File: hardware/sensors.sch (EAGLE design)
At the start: 28 parts, among them J1 CDH, J2 OW, J3 DBG, J4 SUN-UART, J5 ADCS, J6 ENV, J7 SUN, U1 DS18B20, U2 DS18B20, U3 DS18B20

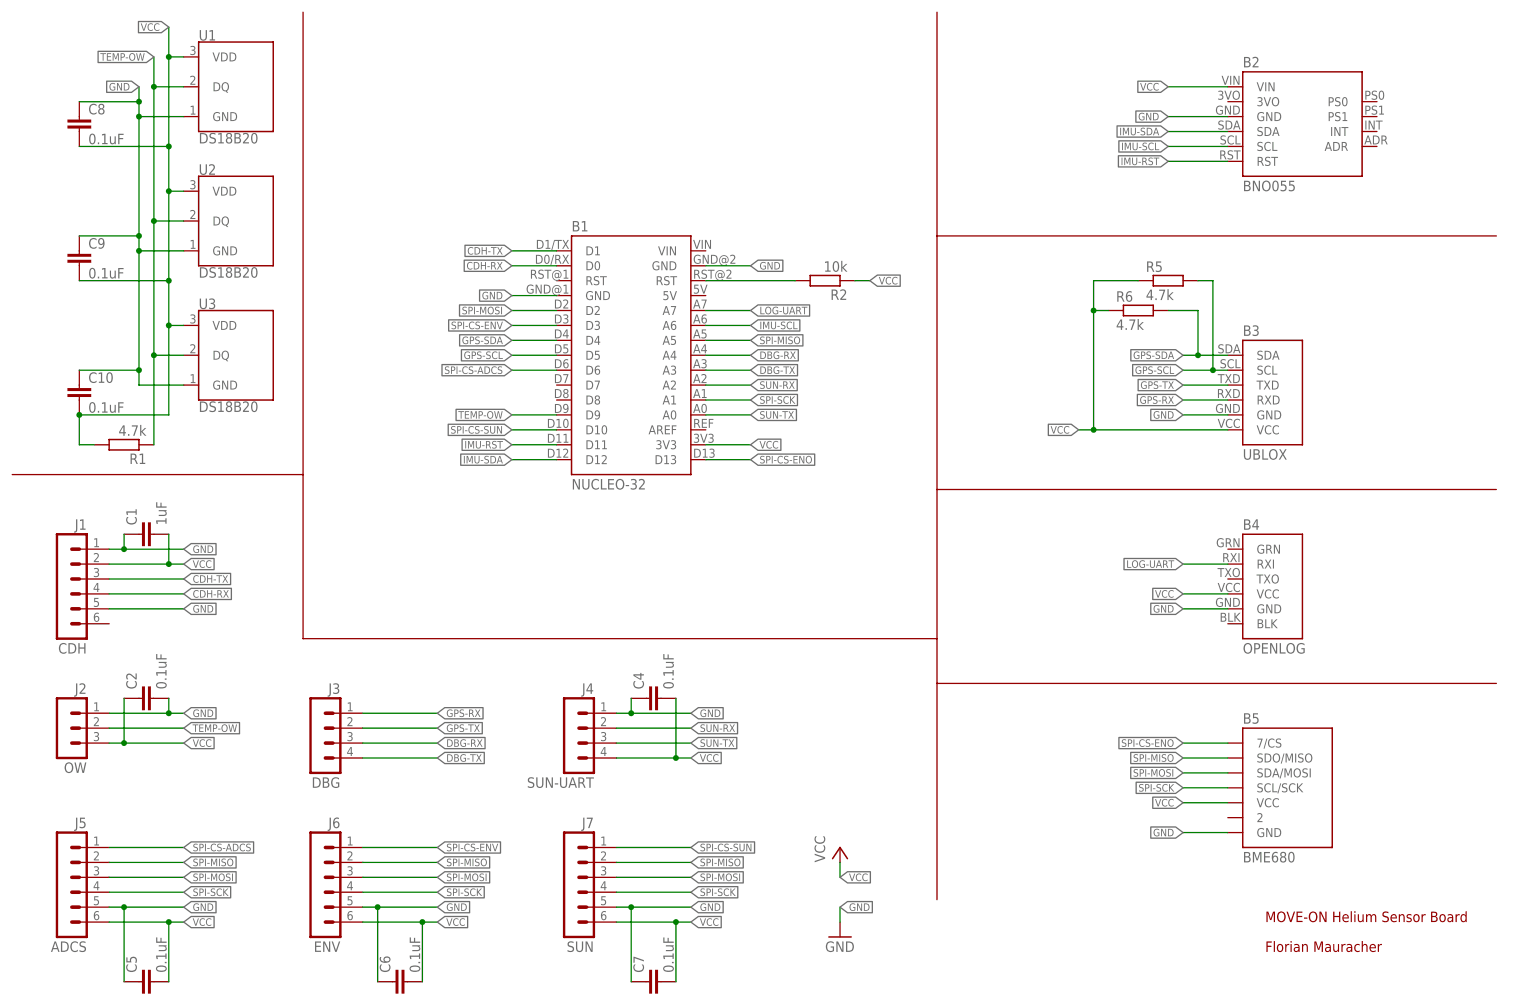
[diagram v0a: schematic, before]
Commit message: Update pin names to match sw
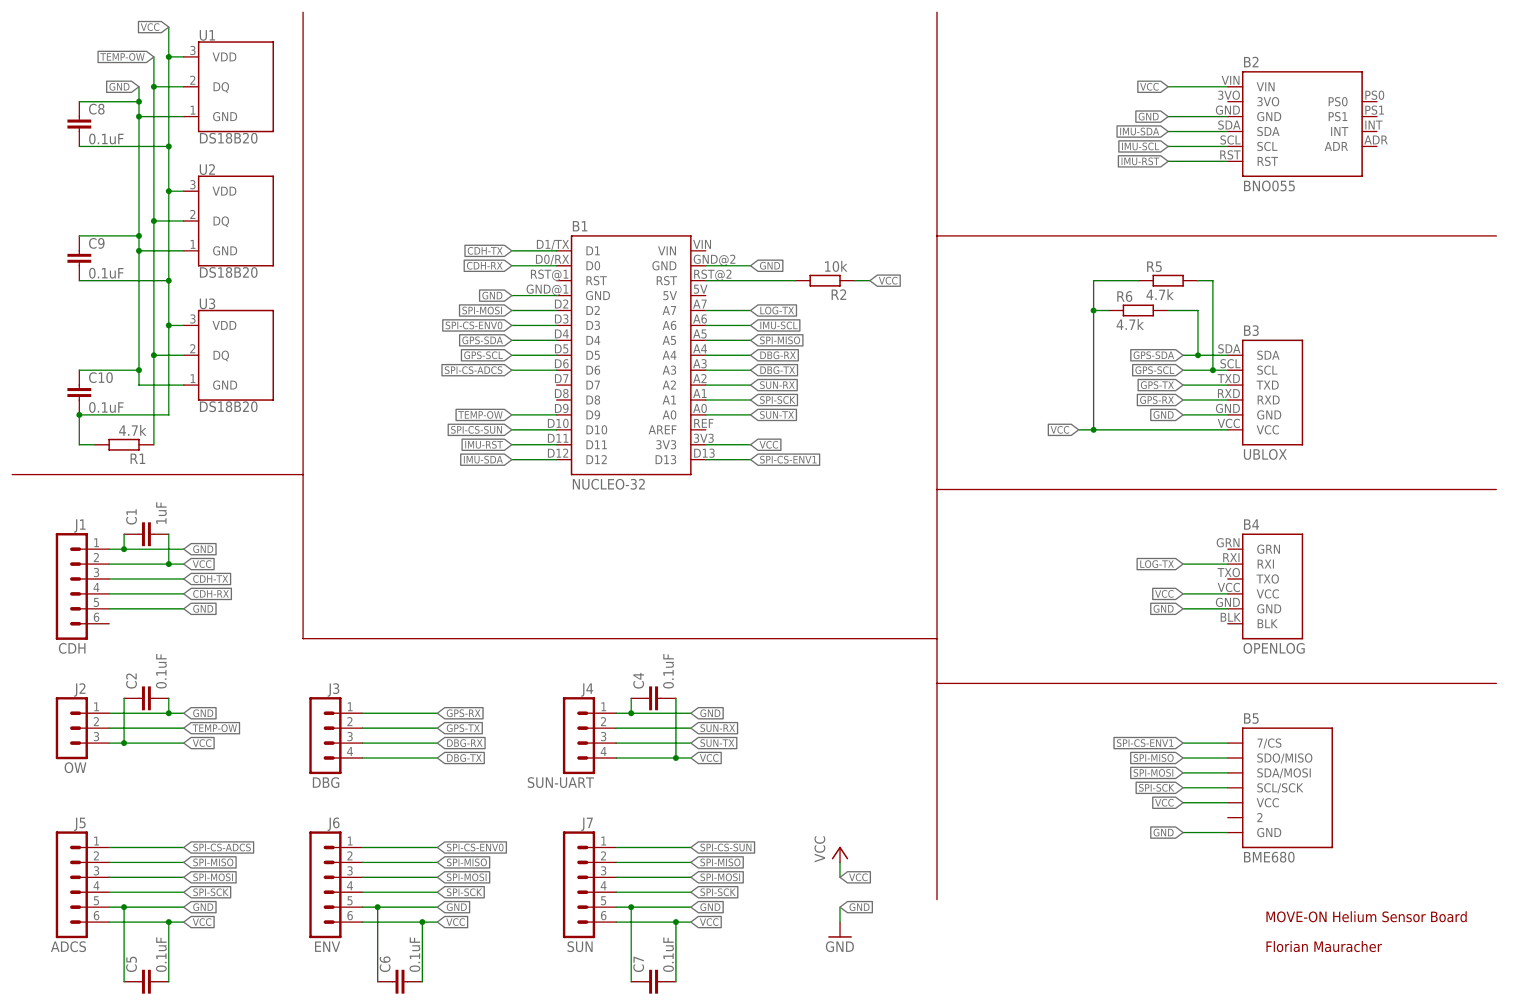
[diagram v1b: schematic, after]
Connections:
- net LOG-UART renamed LOG-TX
- net SPI-CS-ENO renamed SPI-CS-ENV1
- net SPI-CS-ENV renamed SPI-CS-ENV0
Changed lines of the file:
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@@
 </segment>
 </net>
-<net name="LOG-UART" class="0">
+<net name="LOG-TX" class="0">
 <segment>
 <pinref part="B4" gate="G$1" pin="RXI"/>
@@
 </segment>
 </net>
-<net name="SPI-CS-ENV" class="0">
+<net name="SPI-CS-ENV0" class="0">
 <segment>
 <pinref part="B1" gate="G$1" pin="D3"/>
@@
 </segment>
 </net>
-<net name="SPI-CS-ENO" class="0">
+<net name="SPI-CS-ENV1" class="0">
 <segment>
 <pinref part="B1" gate="G$1" pin="D13"/>

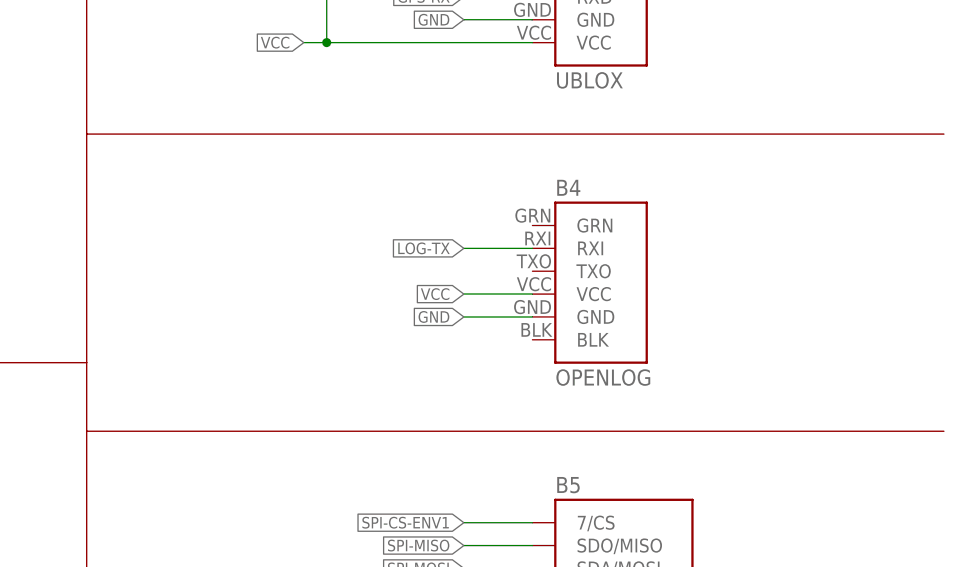
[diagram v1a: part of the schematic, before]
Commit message: Add HM-11 module as alternative to OpenLog
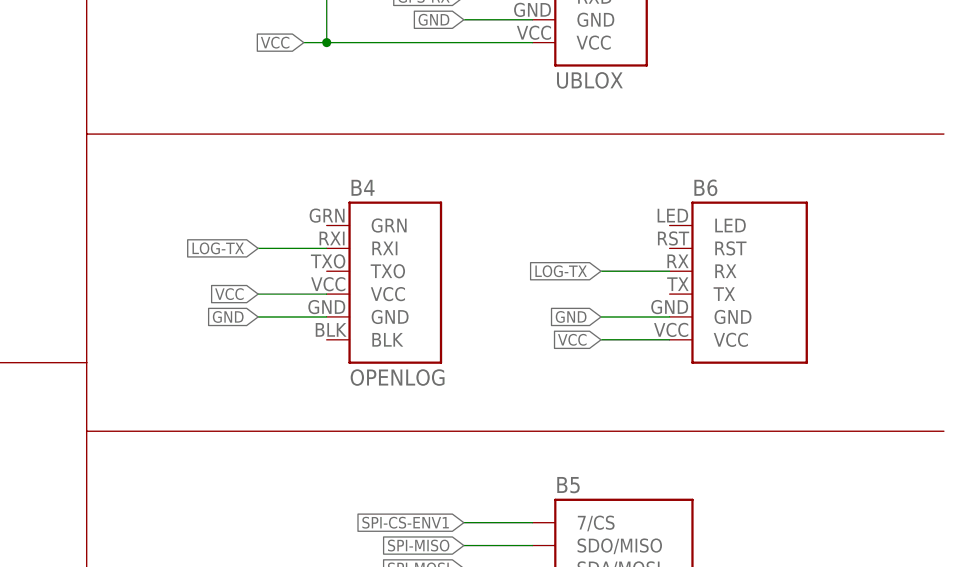
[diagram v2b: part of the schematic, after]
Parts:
- added B6: (no value), Frcy:HUAMAO-HM-11BO
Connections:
- net GND: now also B6.GND
- net LOG-TX: now also B6.RX
- net VCC: now also B6.VCC
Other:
- moved on the sheet: B4
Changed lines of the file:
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@@
 <part name="C9" library="rcl" library_urn="urn:adsk.eagle:library:334" deviceset="C-EU" device="C2012" package3d_urn="urn:adsk.eagle:package:23625/2" value="0.1uF"/>
 <part name="C10" library="rcl" library_urn="urn:adsk.eagle:library:334" deviceset="C-EU" device="C2012" package3d_urn="urn:adsk.eagle:package:23625/2" value="0.1uF"/>
+<part name="B6" library="Frcy" deviceset="HUAMAO-HM-11" device="BO"/>
 </parts>
 <sheets>
@@
 <instance part="GND1" gate="1" x="144.78" y="17.78"/>
 <instance part="B3" gate="G$1" x="215.9" y="109.22"/>
-<instance part="B4" gate="G$1" x="218.44" y="76.2"/>
+<instance part="B4" gate="G$1" x="195.58" y="76.2"/>
 <instance part="J2" gate="G$1" x="15.24" y="53.34" rot="MR0"/>
 <instance part="J3" gate="G$1" x="58.42" y="53.34" rot="MR0"/>
@@
 <instance part="C9" gate="G$1" x="15.24" y="134.62"/>
 <instance part="C10" gate="G$1" x="15.24" y="111.76"/>
+<instance part="B6" gate="G$1" x="233.68" y="78.74"/>
 </instances>
 <busses>
@@
 <segment>
 <pinref part="B4" gate="G$1" pin="VCC"/>
-<wire x1="210.82" y1="76.2" x2="203.2" y2="76.2" width="0.1524" layer="91"/>
-<label x="203.2" y="76.2" size="1.27" layer="95" rot="R180" xref="yes"/>
+<wire x1="187.96" y1="76.2" x2="180.34" y2="76.2" width="0.1524" layer="91"/>
+<label x="180.34" y="76.2" size="1.27" layer="95" rot="R180" xref="yes"/>
 </segment>
 <segment>
@@
 <junction x="73.66" y="20.32"/>
 </segment>
+<segment>
+<pinref part="B6" gate="G$1" pin="VCC"/>
+<wire x1="226.06" y1="71.12" x2="218.44" y2="71.12" width="0.1524" layer="91"/>
+<label x="218.44" y="71.12" size="1.27" layer="95" rot="R180" xref="yes"/>
+</segment>
 </net>
 <net name="GND" class="0">
@@
 <segment>
 <pinref part="B4" gate="G$1" pin="GND"/>
-<wire x1="210.82" y1="73.66" x2="203.2" y2="73.66" width="0.1524" layer="91"/>
-<label x="203.2" y="73.66" size="1.27" layer="95" rot="R180" xref="yes"/>
+<wire x1="187.96" y1="73.66" x2="180.34" y2="73.66" width="0.1524" layer="91"/>
+<label x="180.34" y="73.66" size="1.27" layer="95" rot="R180" xref="yes"/>
 </segment>
 <segment>
@@
 <junction x="109.22" y="22.86"/>
 </segment>
+<segment>
+<pinref part="B6" gate="G$1" pin="GND"/>
+<wire x1="226.06" y1="73.66" x2="218.44" y2="73.66" width="0.1524" layer="91"/>
+<label x="218.44" y="73.66" size="1.27" layer="95" rot="R180" xref="yes"/>
+</segment>
 </net>
 <net name="IMU-SDA" class="0">
@@
 <segment>
 <pinref part="B4" gate="G$1" pin="RXI"/>
-<wire x1="210.82" y1="81.28" x2="203.2" y2="81.28" width="0.1524" layer="91"/>
-<label x="203.2" y="81.28" size="1.27" layer="95" rot="R180" xref="yes"/>
+<wire x1="187.96" y1="81.28" x2="180.34" y2="81.28" width="0.1524" layer="91"/>
+<label x="180.34" y="81.28" size="1.27" layer="95" rot="R180" xref="yes"/>
 </segment>
 <segment>
@@
 <label x="129.54" y="124.46" size="1.27" layer="95" xref="yes"/>
 </segment>
-</net>
+<segment>
+<pinref part="B6" gate="G$1" pin="RX"/>
+<wire x1="226.06" y1="78.74" x2="218.44" y2="78.74" width="0.1524" layer="91"/>
+<label x="218.44" y="78.74" size="1.27" layer="95" rot="R180" xref="yes"/>
+</segment>
+</net>
